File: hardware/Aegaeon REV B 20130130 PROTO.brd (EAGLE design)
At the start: 9.2 x 15.2 mm, 39 parts, among them IC1 ATTINY84A-MMH, Q1 DMN65D8LDW, U1 V_REG_LDOSMD

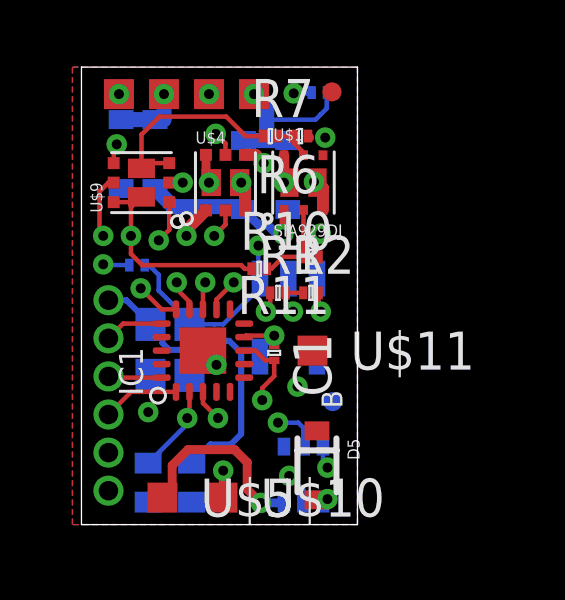
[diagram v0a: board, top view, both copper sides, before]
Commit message: Initial commit for H-Bridge designed with SI5504DC parts.
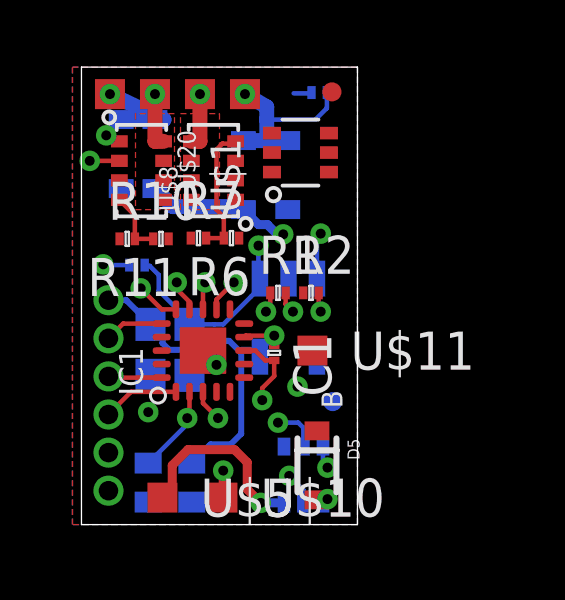
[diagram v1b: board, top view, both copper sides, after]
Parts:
- removed U$4, U$9: SSM6N55NU, Railstars:UDFN6
- added U$20, U$8: SI5504DC, Railstars:1206-8
- U$1: value SIA929DJ -> DMN65D8LDW; device Railstars:SC70-6L -> Railstars:SOT363
- moved R11 5.04 mm to (2.95, 9.53)
- moved R10 4.51 mm to (1.82, 9.53)
- moved R7 4.16 mm to (4.20, 9.55)
- moved R6 4.10 mm to (5.30, 9.55)
- moved DCC_L 1.80 mm to (1.25, 14.3)
- moved U$3 1.20 mm to (2.75, 14.3)
- moved U$1 1.00 mm to (7.60, 12.4), turned to 90 degrees
- moved DCC_R 0.30 mm to (5.75, 14.3)
- moved U$2 0.30 mm to (4.25, 14.3)
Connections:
- net FORWARD: now also U$1.P$2, U$20.P$2; no longer U$4.G1, U$9.G2
- net GND: now also U$20.P$1, U$8.P$1; no longer U$4.S1, U$4.S2
- net MOTOR_L: now also U$20.P$5, U$20.P$6, U$20.P$7, U$20.P$8; no longer U$1.D1, U$1.D1$2, U$4.D1, U$4.D1$1
- net MOTOR_R: now also U$8.P$5, U$8.P$6, U$8.P$7, U$8.P$8; no longer U$1.D2, U$1.D2$2, U$4.D2, U$4.D2$2
- net N$1: now also U$8.P$4; no longer U$1.G2
- net N$10: now also U$1.P$1; no longer U$9.D1, U$9.D1$1
- net N$11: now also U$1.P$4; no longer U$9.D2, U$9.D2$2
- net N$4: now also U$20.P$4; no longer U$1.G1
- net PWM: now also U$1.P$3, U$1.P$6; no longer U$9.S1, U$9.S2
- net REVERSE: now also U$1.P$5, U$8.P$2; no longer U$4.G2, U$9.G1
- net VDCC: now also U$20.P$3, U$8.P$3; no longer U$1.S1, U$1.S2
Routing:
- net MOTOR_L: track 15.3 -> 3.87 mm, vias 4 -> 2
- net DCC_L_LL: track 15.9 -> 7.09 mm, vias 2 -> 1
- net FORWARD: track 11.0 -> 2.45 mm, vias 3 -> 2
- net PWM: track 8.59 -> 1.08 mm, vias 3 -> 1
- net MOTOR_R: track 14.5 -> 7.19 mm, vias 4 -> 2
- net N$10: track 7.27 -> 0.00 mm, vias 1 -> 0
- net N$11: track 6.69 -> 0.00 mm
- net REVERSE: track 9.67 -> 3.09 mm, vias 3 -> 1
- net N$1: track 1.27 -> 4.39 mm
- net GND: track 5.51 -> 4.13 mm, vias 6 -> 5
- net DCC_L: track 2.27 -> 3.42 mm
- net N$4: track 2.95 -> 2.13 mm
- net BEMF: track 10.4 -> 9.85 mm
- net VDCC: track 6.30 -> 5.79 mm, vias 4 -> 3
- added copper zone on layer 1, net MOTOR_L
- added copper zone on layer 1, net MOTOR_R

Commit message: Working on the layout a bit? Lost track of where I was.
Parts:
- moved D1 1.22 mm to (2.62, 11.7)
- moved D2 1.22 mm to (3.75, 11.7)
- moved R5 1.05 mm to (7.17, 14.4), turned to 0 degrees
- moved U$1 0.60 mm to (7.60, 11.8), turned to 0 degrees
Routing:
- net REVERSE: track 3.09 -> 5.94 mm
- net DCC_R: track 6.12 -> 4.22 mm
- net VDCC: track 5.79 -> 4.50 mm

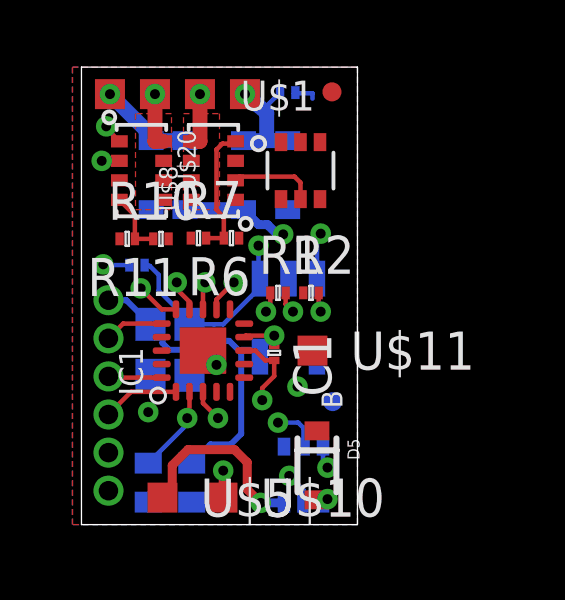
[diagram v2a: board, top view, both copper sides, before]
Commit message: Redesigning the H-Bridge. This one seems to work under test.
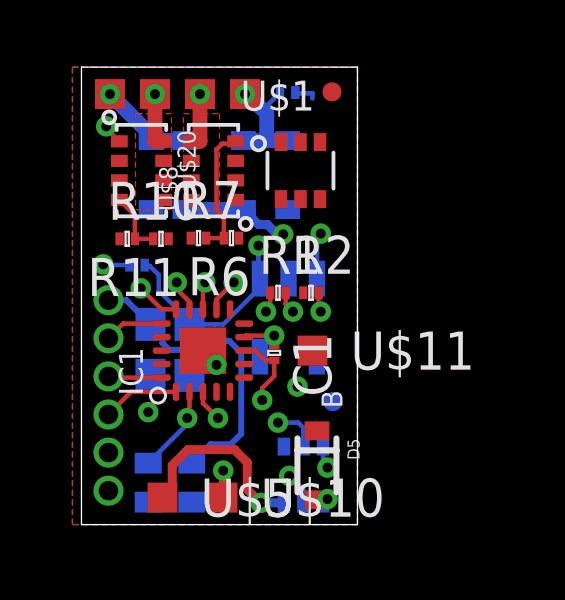
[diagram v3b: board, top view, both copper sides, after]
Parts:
- R10, R7: value 470 -> 1K
- R11, R6: value 10K -> 1K
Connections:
- removed net PWM: IC1.P$14, U$1.P$3, U$1.P$6
- new net FWD_PWM: IC1.P$15, U$20.P$2
- new net REV_PWM: IC1.P$14, U$8.P$2
- net FORWARD: now also IC1.P$11, U$1.P$5; no longer IC1.P$15, U$1.P$2, U$20.P$2
- net GND: now also U$1.P$3, U$1.P$6
- net N$10: now also U$1.P$4; no longer U$1.P$1
- net N$11: now also U$1.P$1; no longer U$1.P$4
- net REVERSE: now also U$1.P$2; no longer U$1.P$5, U$8.P$2
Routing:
- net REVERSE: track 5.94 -> 3.09 mm
- net FORWARD: track 2.05 -> 0.00 mm, vias 2 -> 0
- net FWD_PWM: track 0.00 -> 1.46 mm, vias 0 -> 1
- net REV_PWM: track 0.00 -> 1.08 mm, vias 0 -> 1
- net PWM: track 1.08 -> 0.00 mm, vias 1 -> 0
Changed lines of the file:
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@@
 <element name="C2" library="rcl" package="C0402" value=".1uF" x="2.525" y="1.4" rot="MR270"/>
 <element name="C4" library="rcl" package="CPOL0603" value="47uF" x="2.6" y="5.825" rot="MR270"/>
-<element name="R6" library="rcl" package="R0201" value="10K" x="5.3" y="9.55" rot="R180"/>
-<element name="R7" library="rcl" package="R0201" value="470" x="4.2" y="9.55"/>
-<element name="R10" library="rcl" package="R0201" value="470" x="1.825" y="9.525"/>
-<element name="R11" library="rcl" package="R0201" value="10K" x="2.95" y="9.525" rot="R180"/>
+<element name="R6" library="rcl" package="R0201" value="1K" x="5.3" y="9.55" rot="R180"/>
+<element name="R7" library="rcl" package="R0201" value="1K" x="4.2" y="9.55"/>
+<element name="R10" library="rcl" package="R0201" value="1K" x="1.825" y="9.525"/>
+<element name="R11" library="rcl" package="R0201" value="1K" x="2.95" y="9.525" rot="R180"/>
 <element name="U1" library="SparkFun-PowerIC" package="SOT23-5" value="V_REG_LDOSMD" x="7.2" y="6.9" rot="MR180"/>
 <element name="D5" library="SparkFun-DiscreteSemi" package="SOD-323" value="MM3Z27VT1G" x="8.15" y="1.975" rot="R270"/>
@@
 <wire x1="1.5635" y1="12.775" x2="1.125" y2="13.2135" width="0.1524" layer="1"/>
 <wire x1="1.125" y1="13.2135" x2="1.125" y2="13.275" width="0.1524" layer="1"/>
-<wire x1="7.175" y1="10.5" x2="5.4365" y2="10.825" width="0" layer="19" extent="1-16"/>
+<contactref element="U$1" pad="P$3"/>
+<contactref element="U$1" pad="P$6"/>
+<wire x1="6.95" y1="10.85" x2="8.25" y2="12.75" width="0" layer="19" extent="1-1"/>
+<wire x1="7.175" y1="10.5" x2="6.95" y2="10.85" width="0" layer="19" extent="1-16"/>
+<wire x1="5.4365" y1="10.825" x2="6.95" y2="10.85" width="0" layer="19" extent="1-1"/>
 </signal>
 <signal name="DCC_L">
@@
 <wire x1="4.8" y1="7.175" x2="4.8" y2="7.5" width="0.1524" layer="1"/>
 <wire x1="4.8" y1="7.5" x2="5.375" y2="8.075" width="0.1524" layer="1"/>
-<contactref element="U$1" pad="P$5"/>
-<contactref element="U$8" pad="P$2"/>
-<wire x1="5.4365" y1="11.475" x2="5.5615" y2="11.6" width="0.1524" layer="1"/>
-<wire x1="5.5615" y1="11.6" x2="7.4" y2="11.6" width="0.1524" layer="1"/>
-<wire x1="7.4" y1="11.6" x2="7.6" y2="11.4" width="0.1524" layer="1"/>
-<wire x1="7.6" y1="11.4" x2="7.6" y2="10.85" width="0.1524" layer="1"/>
-<wire x1="5.3" y1="10" x2="5.4365" y2="11.475" width="0" layer="19" extent="1-9"/>
-</signal>
-<signal name="FORWARD">
+<contactref element="U$1" pad="P$2"/>
+<wire x1="5.3" y1="10" x2="7.6" y2="12.75" width="0" layer="19" extent="1-9"/>
+</signal>
+<signal name="FWD_PWM">
 <contactref element="IC1" pad="P$15"/>
 <via x="2.275" y="7.875" extent="1-16" drill="0.3302"/>
 <wire x1="3.45" y1="7.175" x2="2.975" y2="7.175" width="0.1524" layer="1"/>
 <wire x1="2.975" y1="7.175" x2="2.275" y2="7.875" width="0.1524" layer="1"/>
-<contactref element="U$1" pad="P$2"/>
 <contactref element="U$20" pad="P$2"/>
-<via x="0.975" y="12.125" extent="1-16" drill="0.3302"/>
-<wire x1="0.975" y1="12.125" x2="1.5635" y2="12.125" width="0.1524" layer="1"/>
-<wire x1="1.5635" y1="12.125" x2="7.6" y2="12.75" width="0" layer="19" extent="1-1"/>
 <wire x1="2.275" y1="7.875" x2="1.5635" y2="12.125" width="0" layer="19" extent="1-1"/>
 </signal>
@@
 <signal name="N$10">
 <contactref element="R10" pad="1"/>
-<contactref element="U$1" pad="P$1"/>
-<wire x1="1.57" y1="9.525" x2="6.95" y2="12.75" width="0" layer="19" extent="1-1"/>
+<contactref element="U$1" pad="P$4"/>
+<wire x1="1.57" y1="9.525" x2="8.25" y2="10.85" width="0" layer="19" extent="1-1"/>
 </signal>
 <signal name="N$11">
 <contactref element="R7" pad="1"/>
-<contactref element="U$1" pad="P$4"/>
-<wire x1="3.945" y1="9.55" x2="8.25" y2="10.85" width="0" layer="19" extent="1-1"/>
+<contactref element="U$1" pad="P$1"/>
+<wire x1="3.945" y1="9.55" x2="6.95" y2="12.75" width="0" layer="19" extent="1-1"/>
 </signal>
 <signal name="N$2">
@@
 <wire x1="6.2" y1="8.2001" x2="6.2" y2="9.3" width="0.1524" layer="16"/>
 </signal>
-<signal name="PWM">
+<signal name="REV_PWM">
 <contactref element="IC1" pad="P$14"/>
 <wire x1="3.9" y1="7.175" x2="3.9" y2="7.425" width="0.1524" layer="1"/>
@@
 <wire x1="3.475" y1="7.85" x2="3.475" y2="8.075" width="0.1524" layer="1"/>
 <via x="3.475" y="8.075" extent="1-16" drill="0.3302"/>
-<contactref element="U$1" pad="P$6"/>
-<contactref element="U$1" pad="P$3"/>
-<wire x1="3.475" y1="8.075" x2="6.95" y2="10.85" width="0" layer="19" extent="1-1"/>
-<wire x1="6.95" y1="10.85" x2="8.25" y2="12.75" width="0" layer="19" extent="1-1"/>
+<contactref element="U$8" pad="P$2"/>
+<wire x1="3.475" y1="8.075" x2="5.4365" y2="11.475" width="0" layer="19" extent="1-1"/>
+</signal>
+<signal name="FORWARD">
+<contactref element="IC1" pad="P$11"/>
+<contactref element="U$1" pad="P$5"/>
+<wire x1="5.25" y1="7.175" x2="7.6" y2="10.85" width="0" layer="19" extent="1-1"/>
 </signal>
 </signals>
